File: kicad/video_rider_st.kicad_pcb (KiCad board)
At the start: 2 copper layers, 104 x 92.1 mm, 32 parts, among them J1 F3311A7H121020E200, J2 F3311A7H121020E200, J3 Conn_01x02_Male, J4 Conn_01x03_Male, J5 F3311A7H121020E200, J6 F3311A7H121020E200, J7 Conn_01x06_Male, U1 ST_SHIFTER_PHY, U10 ST_GLUE_SOCKET, U2 ST_SHIFTER_SOCKET, U3 Pico, U4 74HC245, U5 74HC245, U6 74HC245, U7 74HC245, U8 XC95144XL-TQ100, U9 ST_GLUE_PHY, X1 CXO_DIP14

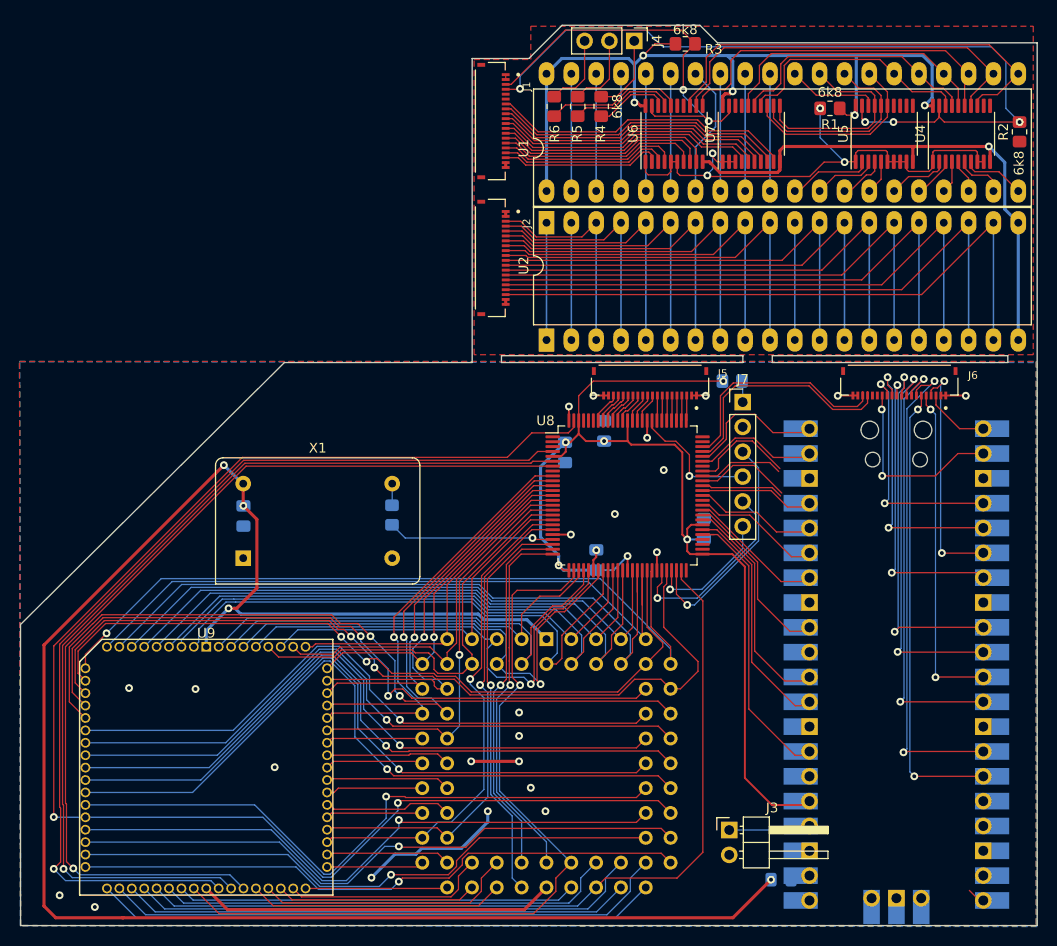
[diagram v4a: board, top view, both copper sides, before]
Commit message: Adding support for other oscillators
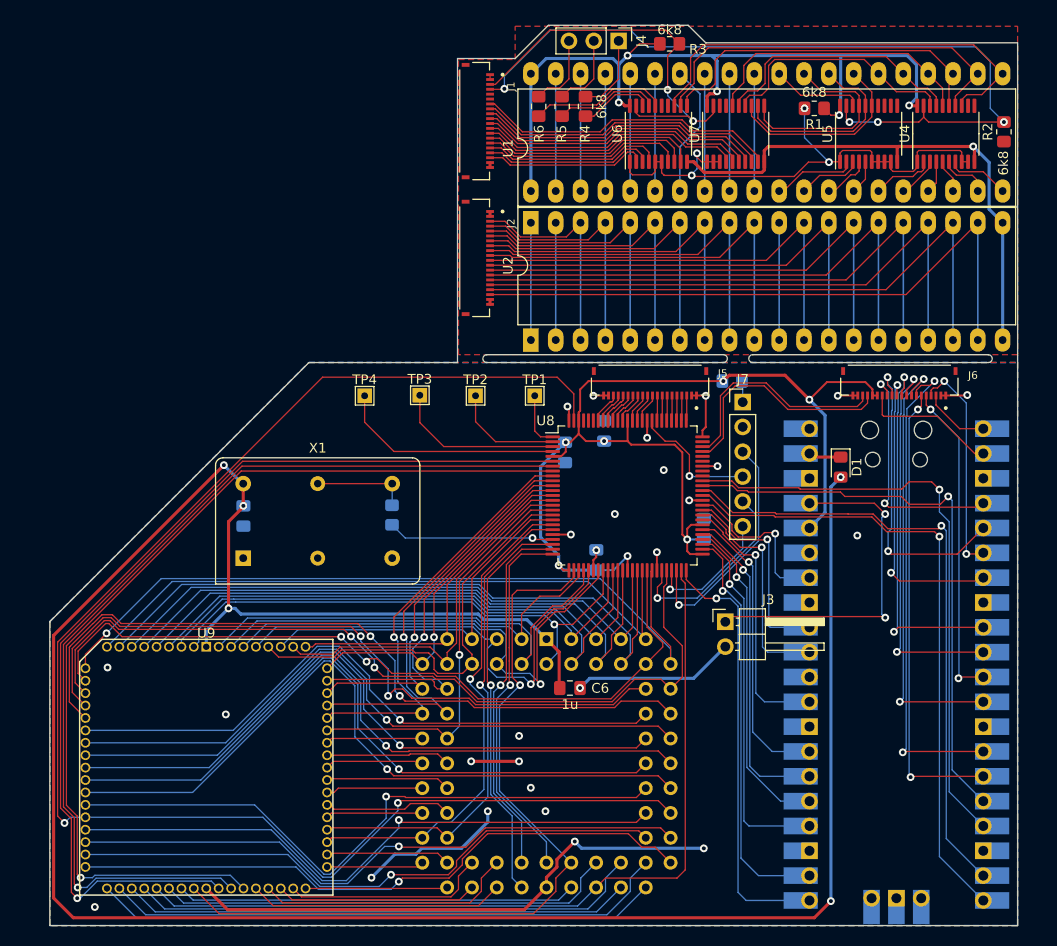
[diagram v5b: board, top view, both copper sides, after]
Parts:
- added C6: 1u, Capacitor_SMD:C_0805_2012Metric_Pad1.18x1.45mm_HandSolder, F.Cu at (152.8, 119.9)
- added TP1: TestPoint, TestPoint:TestPoint_THTPad_1.5x1.5mm_Drill0.7mm, F.Cu at (149.2, 90.0)
- added TP2: TestPoint, TestPoint:TestPoint_THTPad_1.5x1.5mm_Drill0.7mm, F.Cu at (143.2, 90.0)
- added TP3: TestPoint, TestPoint:TestPoint_THTPad_1.5x1.5mm_Drill0.7mm, F.Cu at (137.4, 90.0)
- added TP4: TestPoint, TestPoint:TestPoint_THTPad_1.5x1.5mm_Drill0.7mm, F.Cu at (131.8, 90.0)
- D1: moved to F.Cu
- X1: value CXO_DIP14 -> CXO_DIP14_DIP8_DUAL; footprint Oscillator:Oscillator_DIP-14 -> CXO_Dual_DIP:CXO_Dual_DIP
- moved D1 42.6 mm to (180.5, 97.3), turned to -90 degrees
- moved J3 21.3 mm to (168.7, 113.1)
- moved R2 1.60 mm to (197.2, 63.0)
- moved J1 1.60 mm to (143.1, 61.9)
- moved J2 1.60 mm to (143.1, 75.9)
- moved J4 1.60 mm to (157.8, 53.7)
- moved R1 1.60 mm to (177.8, 60.6)
- moved R3 1.60 mm to (163.0, 54.0)
- moved R4 1.60 mm to (154.4, 60.4)
- moved R5 1.60 mm to (152.0, 60.4)
- moved R6 1.60 mm to (149.6, 60.4)
- moved U1 1.60 mm to (148.8, 72.3)
- moved U2 1.60 mm to (148.8, 84.3)
- moved U4 1.60 mm to (191.3, 63.2)
- moved U5 1.60 mm to (183.4, 63.2)
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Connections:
- J6 pad 15: unconnected-(J6-Pad15) -> /3V3
- J6 pad 16: unconnected-(J6-Pad16) -> /3V3
- U8 pad 1: unconnected-(U8-Pad1) -> /TP1
- U8 pad 2: unconnected-(U8-Pad2) -> /TP2
- U8 pad 3: unconnected-(U8-Pad3) -> /TP3
- U8 pad 4: /BLANK_OUT -> /TP4
- U8 pad 50: unconnected-(U8-Pad50) -> /PICO_D2
- U8 pad 52: unconnected-(U8-Pad52) -> /PICO_D3
- U8 pad 53: unconnected-(U8-Pad53) -> /PICO_D4
- U8 pad 54: unconnected-(U8-Pad54) -> /PICO_D5
- U8 pad 55: /PICO_A2 -> /PICO_D6
- U8 pad 56: /PICO_A1 -> /PICO_D7
- U8 pad 58: /PICO_A0 -> /PICO_CLK
- U8 pad 59: /PICO_CLK -> /PICO_A0
- U8 pad 6: /HSYNC_OUT -> /BLANK_OUT
- U8 pad 60: /PICO_D7 -> /PICO_A1
- U8 pad 61: /PICO_D6 -> /PICO_A2
- U8 pad 63: /PICO_D5 -> /PICO_D1
- U8 pad 64: /PICO_D4 -> /PICO_D0
- U8 pad 67: /PICO_D0 -> unconnected-(U8-Pad67)
- U8 pad 68: /PICO_D1 -> unconnected-(U8-Pad68)
- U8 pad 7: /VSYNC_OUT -> /HSYNC_OUT
- U8 pad 70: /PICO_D3 -> unconnected-(U8-Pad70)
- U8 pad 71: /PICO_D2 -> unconnected-(U8-Pad71)
- U8 pad 76: /D0_C -> /D15_C
- U8 pad 77: /D1_C -> /D14_C
- U8 pad 78: /D2_C -> /D13_C
- U8 pad 79: /D3_C -> /D12_C
- U8 pad 8: unconnected-(U8-Pad8) -> /VSYNC_OUT
- U8 pad 80: /D4_C -> /D11_C
- U8 pad 81: /D5_C -> /D10_C
- U8 pad 82: /D6_C -> /D9_C
- U8 pad 85: /D7_C -> /D8_C
- U8 pad 86: /D8_C -> /D7_C
- U8 pad 87: /D9_C -> /D6_C
- U8 pad 89: /D10_C -> /D5_C
- U8 pad 90: /D11_C -> /D4_C
- U8 pad 91: /D12_C -> /D3_C
- U8 pad 92: /D13_C -> /D2_C
- U8 pad 93: /D14_C -> /D1_C
- U8 pad 94: /D15_C -> /D0_C
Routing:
- net /PICO_D0: track 8.75 -> 63.7 mm, vias 0 -> 1
- net /PICO_D1: track 12.9 -> 65.1 mm, vias 0 -> 1
- net /PICOHSYNC: track 10.1 -> 61.5 mm, vias 0 -> 1
- net /5V_C: track 185.8 -> 236.8 mm, vias 4 -> 5
- net /PICOVSYNC: track 8.52 -> 58.9 mm, vias 0 -> 1
- net /PICO_D2: track 0.00 -> 44.3 mm, vias 0 -> 1
- net /GND_C: track 73.7 -> 117.1 mm, vias 24 -> 27
- net /PICO_D3: track 1.89 -> 41.9 mm, vias 0 -> 1
- net /PICO_D5: track 0.00 -> 33.6 mm, vias 0 -> 1
- net /PICO_D6: track 0.00 -> 32.7 mm, vias 0 -> 1
- net /PICO_D4: track 8.22 -> 37.6 mm, vias 0 -> 1
- net Net-(J3-Pad1): track 11.6 -> 35.7 mm, vias 0 -> 2
- net /TP4: track 0.00 -> 23.2 mm
- net unconnected-(U3-Pad30): track 23.0 -> 0.00 mm
- net /PICO_A0: track 0.00 -> 22.9 mm, vias 0 -> 1
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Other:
- board size 104 x 92.1 mm -> 99 x 92.1 mm

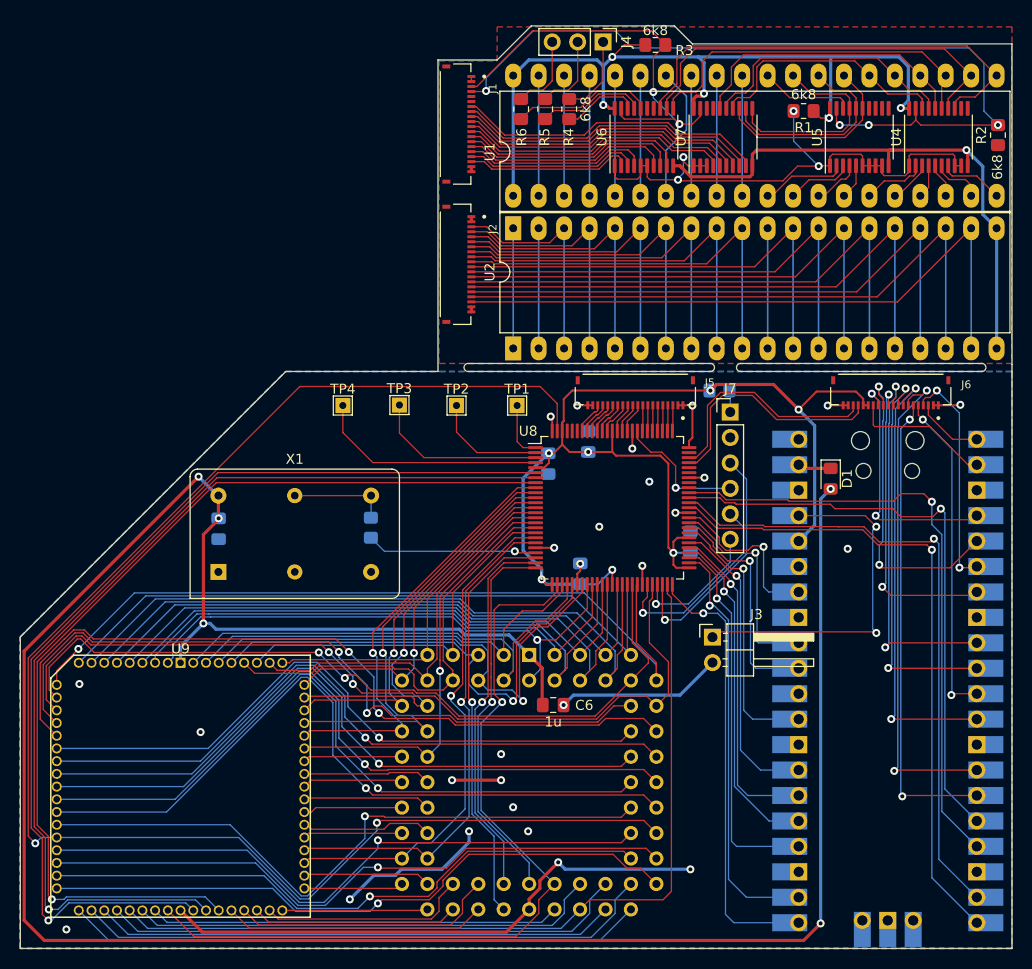
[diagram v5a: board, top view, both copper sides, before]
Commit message: Just about ready to order, but need to check the dual dip library.
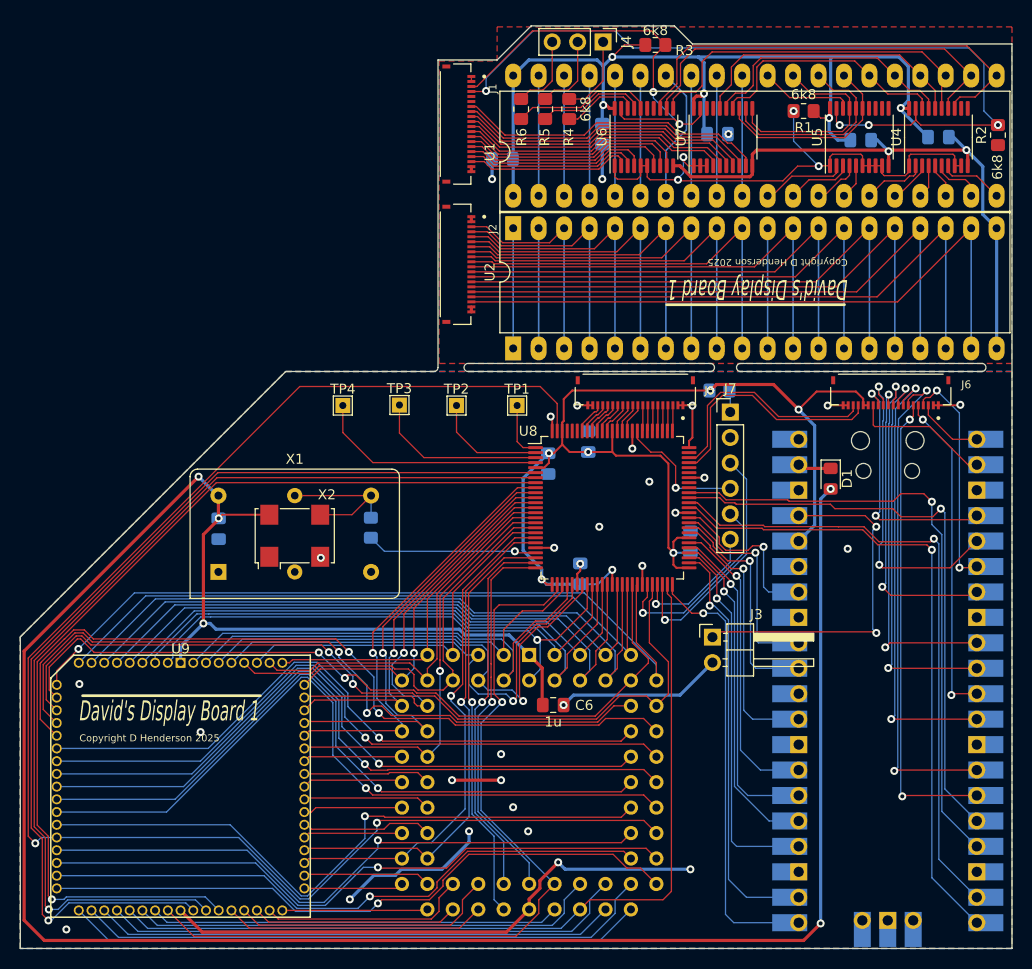
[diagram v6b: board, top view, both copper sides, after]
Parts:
- added C10: 100n, Capacitor_SMD:C_0805_2012Metric_Pad1.18x1.45mm_HandSolder, B.Cu at (169.2, 62.9)
- added C11: 100n, Capacitor_SMD:C_0805_2012Metric_Pad1.18x1.45mm_HandSolder, B.Cu at (157.7, 62.9)
- added C7: 1u, Capacitor_SMD:C_0805_2012Metric_Pad1.18x1.45mm_HandSolder, B.Cu at (147.7, 65.4)
- added C8: 100n, Capacitor_SMD:C_0805_2012Metric_Pad1.18x1.45mm_HandSolder, B.Cu at (191.3, 63.2)
- added C9: 100n, Capacitor_SMD:C_0805_2012Metric_Pad1.18x1.45mm_HandSolder, B.Cu at (183.5, 63.5)
- added X2: IQXO-70, Oscillator:Oscillator_SMD_IQD_IQXO70-4Pin_7.5x5.0mm, F.Cu at (127.0, 103.0)
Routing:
- net /5V: track 82.5 -> 96.4 mm
- net /GND: track 58.5 -> 68.6 mm, vias 1 -> 5
- net /OSC_OUT: track 9.84 -> 15.7 mm
- net /5V_C: track 236.8 -> 242.0 mm
- net /GND_C: vias 27 -> 28
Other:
- outline, holes or cut-outs redrawn
- board text added: "Copyright D Henderson 2025"
- board text added: "~{David's Display Board 1}"
